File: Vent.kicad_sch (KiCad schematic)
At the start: 11 parts, among them J2 B2B-XH-A_LF__SN_, J3 Conn_01x03_Pin, SW1 SW_Push, U1 ESP32-H2-MINI-1

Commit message: feat: Remove BOOT pin connection
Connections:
- net IO9: no longer names the net of U1.23 (GPIO9)
- no-connect marks 12 -> 13
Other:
- sheet ExternalAutoprogramming (Low-Profile Female) ports: added none; removed BOOT
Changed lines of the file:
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@@
+	)
+	(no_connect
+		(at 181.61 87.63)
 	)
 	(no_connect
@@
 	(label "IO12"
 		(at 181.61 90.17 0)
-		(effects
-			(font
-				(size 1.27 1.27)
-			)
-			(justify left bottom)
-		)
-	)
-	(label "IO9"
-		(at 24.13 22.86 180)
-		(effects
-			(font
-				(size 1.27 1.27)
-			)
-			(justify right bottom)
-		)
-	)
-	(label "IO9"
-		(at 181.61 87.63 0)
 		(effects
 			(font
@@
 			)
 		)
-		(pin "BOOT" bidirectional
-			(at 24.13 22.86 180)
-			(effects
-				(font
-					(size 1.27 1.27)
-				)
-				(justify left)
-			)
-		)

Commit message: feat: Disconnect EN pin from external autoprogramming
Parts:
- added C4: 1uF, Capacitor_SMD:C_1206_3216Metric, symbol Device:C_Small
- added R4: 10k, Resistor_SMD:R_0201_0603Metric, symbol Device:R
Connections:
- net +3.3V: now also R4.2
- net EN: no longer U1.8 (EN)
- net GND: now also C4.1
- new net: C4.2, R4.1, U1.8 (EN)

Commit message: feat: Replace autoprogramming symbol with Conn_02x03
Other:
- sheet ExternalAutoprogramming (Low-Profile Female) ports: added none; removed EN
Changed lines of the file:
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@@
-		)
-	)
-	(label "EN"
-		(at 24.13 25.4 180)
-		(effects
-			(font
-				(size 1.27 1.27)
-			)
-			(justify right bottom)
 		)
 	)
@@
 			)
 		)
-		(pin "EN" input
-			(at 24.13 25.4 180)
-			(effects
-				(font
-					(size 1.27 1.27)
-				)
-				(justify left)
-			)
-		)

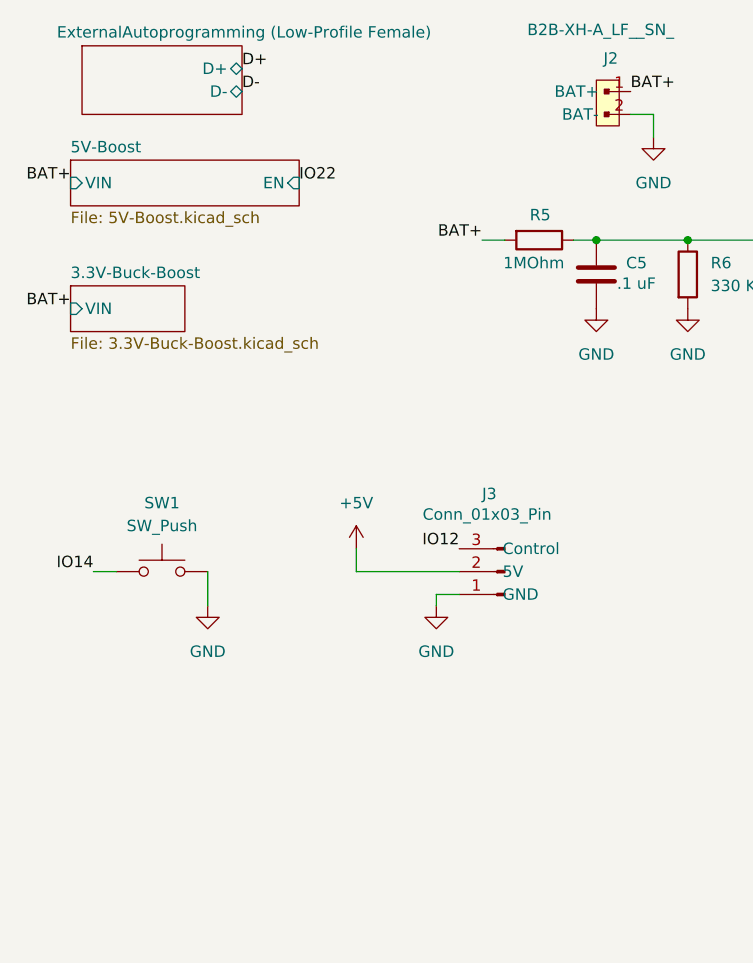
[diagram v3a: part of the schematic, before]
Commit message: feat: Remove autoprogramming schematic
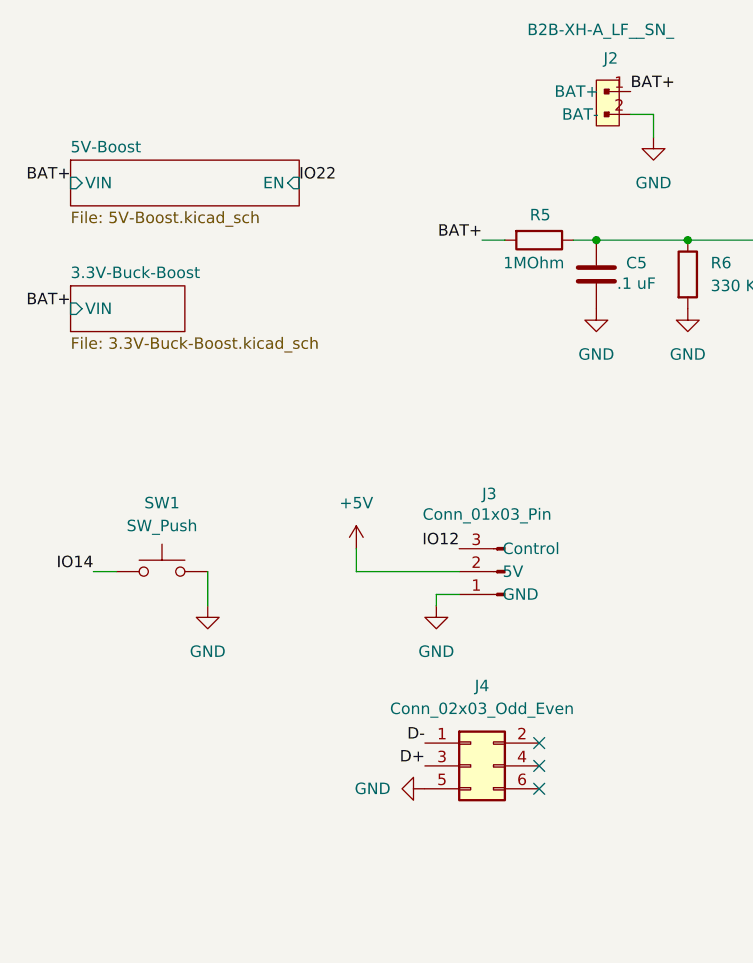
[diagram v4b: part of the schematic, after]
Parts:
- added J4: Conn_02x03_Odd_Even, Connector:Tag-Connect_TC2030-IDC-NL_2x03_P1.27mm_Vertical, symbol Connector_Generic:Conn_02x03_Odd_Even
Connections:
- net D+: now also J4.3 (Pin_3)
- net D-: now also J4.1 (Pin_1)
- net GND: now also J4.5 (Pin_5)
- no-connect marks 13 -> 16
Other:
- removed sheet ExternalAutoprogramming (Low-Profile Female)
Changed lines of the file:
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@@
+	)
+	(no_connect
+		(at 74.93 102.87)
 	)
 	(no_connect
 		(at 181.61 45.72)
+	)
+	(no_connect
+		(at 74.93 97.79)
+	)
+	(no_connect
+		(at 74.93 100.33)
 	)
 	(no_connect
@@
 	)
 	(label "D+"
-		(at 41.91 22.86 0)
+		(at 62.23 100.33 180)
 		(effects
 			(font
 				(size 1.27 1.27)
 			)
-			(justify left bottom)
+			(justify right bottom)
 		)
 	)
@@
 	)
 	(label "D-"
-		(at 41.91 25.4 0)
+		(at 62.23 97.79 180)
 		(effects
 			(font
 				(size 1.27 1.27)
 			)
-			(justify left bottom)
+			(justify right bottom)
 		)
 	)
@@
 	)
 	(symbol
+		(lib_name "Conn_02x03_Odd_Even_1")
+		(lib_id "Connector_Generic:Conn_02x03_Odd_Even")
+		(at 67.31 100.33 0)
+		(unit 1)
+		(body_style 1)
+		(exclude_from_sim no)
+		(in_bom yes)
+		(on_board yes)
+		(in_pos_files yes)
+		(dnp no)
+		(fields_autoplaced yes)
+		(property "Reference" "J4"
+			(at 68.58 91.44 0)
+			(show_name no)
+			(do_not_autoplace no)
+			(effects
+				(font
+					(size 1.27 1.27)
+				)
+			)
+		)
+		(property "Value" "Conn_02x03_Odd_Even"
+			(at 68.58 93.98 0)
+			(show_name no)
+			(do_not_autoplace no)
+			(effects
+				(font
+					(size 1.27 1.27)
+				)
+			)
+		)
+		(property "Footprint" "Connector:Tag-Connect_TC2030-IDC-NL_2x03_P1.27mm_Vertical"
+			(at 67.31 100.33 0)
+			(hide yes)
+			(show_name no)
+			(do_not_autoplace no)
+			(effects
+				(font
+					(size 1.27 1.27)
+				)
+			)
+		)
+		(property "Datasheet" ""
+			(at 67.31 100.33 0)
+			(hide yes)
+			(show_name no)
+			(do_not_autoplace no)
+			(effects
+				(font
+					(size 1.27 1.27)
+				)
+			)
+		)
+		(property "Description" "Generic connector, double row, 02x03, odd/even pin numbering scheme (row 1 odd numbers, row 2 even numbers), script generated (kicad-library-utils/schlib/autogen/connector/)"
+			(at 67.31 100.33 0)
+			(hide yes)
+			(show_name no)
+			(do_not_autoplace no)
+			(effects
+				(font
+					(size 1.27 1.27)
+				)
+			)
+		)
+		(pin "4"
+		)
+		(pin "5"
+		)
+		(pin "2"
+		)
+		(pin "6"
+		)
+		(pin "1"
+		)
+		(pin "3"
+		)
+		(instances
+			(project "Vent"
+				(path "/44080430-3c3a-4a58-87da-65c26034d41d"
+					(reference "J4")
+					(unit 1)
+				)
+			)
+		)
+	)
+	(symbol
 		(lib_id "power:GND")
 		(at 91.44 49.53 0)
@@
 				(path "/44080430-3c3a-4a58-87da-65c26034d41d"
 					(reference "#PWR04")
+					(unit 1)
+				)
+			)
+		)
+	)
+	(symbol
+		(lib_id "power:GND")
+		(at 62.23 102.87 270)
+		(mirror x)
+		(unit 1)
+		(body_style 1)
+		(exclude_from_sim no)
+		(in_bom yes)
+		(on_board yes)
+		(in_pos_files yes)
+		(dnp no)
+		(fields_autoplaced yes)
+		(property "Reference" "#PWR015"
+			(at 55.88 102.87 0)
+			(hide yes)
+			(show_name no)
+			(do_not_autoplace no)
+			(effects
+				(font
+					(size 1.27 1.27)
+				)
+			)
+		)
+		(property "Value" "GND"
+			(at 58.42 102.8699 90)
+			(show_name no)
+			(do_not_autoplace no)
+			(effects
+				(font
+					(size 1.27 1.27)
+				)
+				(justify right)
+			)
+		)
+		(property "Footprint" ""
+			(at 62.23 102.87 0)
+			(hide yes)
+			(show_name no)
+			(do_not_autoplace no)
+			(effects
+				(font
+					(size 1.27 1.27)
+				)
+			)
+		)
+		(property "Datasheet" ""
+			(at 62.23 102.87 0)
+			(hide yes)
+			(show_name no)
+			(do_not_autoplace no)
+			(effects
+				(font
+					(size 1.27 1.27)
+				)
+			)
+		)
+		(property "Description" "Power symbol creates a global label with name \"GND\" , ground"
+			(at 62.23 102.87 0)
+			(hide yes)
+			(show_name no)
+			(do_not_autoplace no)
+			(effects
+				(font
+					(size 1.27 1.27)
+				)
+			)
+		)
+		(pin "1"
+		)
+		(instances
+			(project "Vent"
+				(path "/44080430-3c3a-4a58-87da-65c26034d41d"
+					(reference "#PWR015")
 					(unit 1)
 				)
@@
 				)
 			)
-		)
-	)
-	(sheet
-		(at 24.13 20.32)
-		(size 17.78 7.62)
-		(exclude_from_sim no)
-		(in_bom yes)
-		(on_board yes)
-		(dnp no)
-		(stroke
-			(width 0.1524)
-			(type solid)
-		)
-		(fill
-			(color 255 255 194 1)
-		)
-		(property "Sheetname" "ExternalAutoprogramming (Low-Profile Female)"
-			(at 21.336 19.558 0)
-			(show_name no)
-			(do_not_autoplace no)
-			(effects
-				(font
-					(size 1.27 1.27)
-				)
-				(justify left bottom)
-			)
-		)
-		(property "Sheetfile" "ExternalAutoprogramming.kicad_sch"
-			(at 12.446 28.448 0)
-			(hide yes)
-			(show_name no)
-			(do_not_autoplace no)
-			(effects
-				(font
-					(size 1.27 1.27)
-				)
-				(justify left top)
-			)
-		)
-		(pin "D+" bidirectional
-			(at 41.91 22.86 0)
-			(effects
-				(font
-					(size 1.27 1.27)
-				)
-				(justify right)
-			)
-		)
-		(pin "D-" bidirectional
-			(at 41.91 25.4 0)
-			(effects
-				(font
-					(size 1.27 1.27)
-				)
-				(justify right)
-			)
-		)
-		(instances
-			(project "Vent"
-				(path "/44080430-3c3a-4a58-87da-65c26034d41d"
-					(page "2")
-				)
-			)

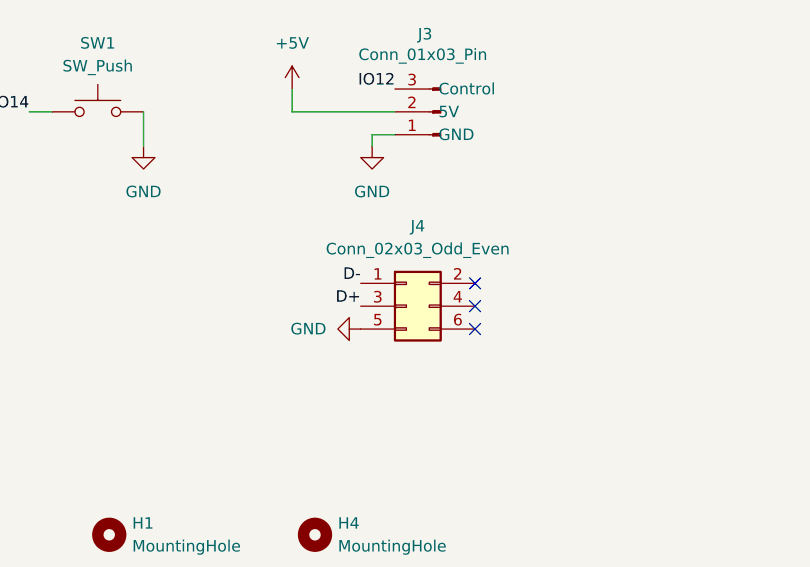
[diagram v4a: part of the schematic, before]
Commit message: feat: Use 1x3 male pin header rather than Tag-Connect
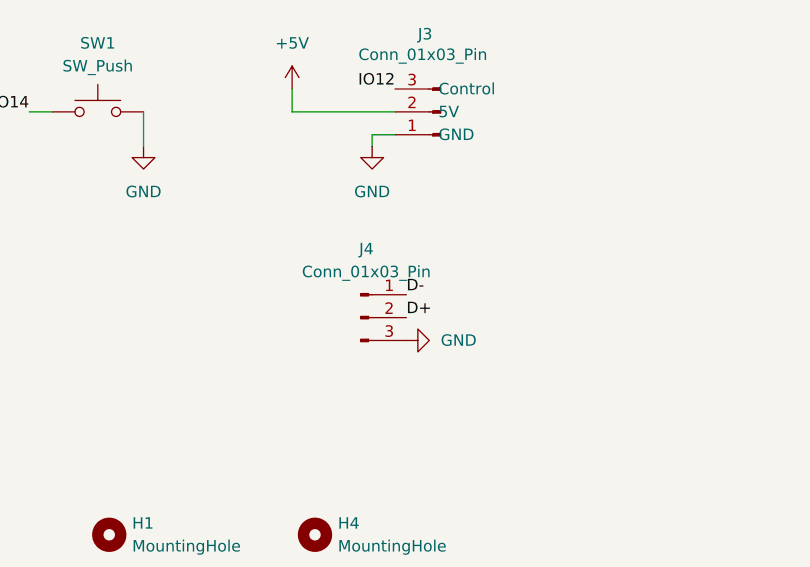
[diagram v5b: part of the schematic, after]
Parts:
- removed J4: Conn_02x03_Odd_Even, Connector:Tag-Connect_TC2030-IDC-NL_2x03_P1.27mm_Vertical, symbol Connector_Generic:Conn_02x03_Odd_Even
- added J4: Conn_01x03_Pin, Connector_PinHeader_2.54mm:PinHeader_1x03_P2.54mm_Vertical, symbol Connector:Conn_01x03_Pin
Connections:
- net D+: now also J4.2 (Pin_2)
- net D-: now also J4.1 (Pin_1)
- net GND: now also J4.3 (Pin_3)
- no-connect marks 16 -> 13
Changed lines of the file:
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@@
-	)
-	(no_connect
-		(at 74.93 102.87)
 	)
 	(no_connect
 		(at 181.61 45.72)
-	)
-	(no_connect
-		(at 74.93 97.79)
-	)
-	(no_connect
-		(at 74.93 100.33)
 	)
 	(no_connect
@@
 		)
 	)
-	(label "D+"
-		(at 62.23 100.33 180)
-		(effects
-			(font
-				(size 1.27 1.27)
-			)
-			(justify right bottom)
-		)
-	)
 	(label "IO14"
 		(at 111.76 55.88 180)
@@
 		)
 	)
+	(label "D-"
+		(at 67.31 99.06 0)
+		(effects
+			(font
+				(size 1.27 1.27)
+			)
+			(justify left bottom)
+		)
+	)
 	(label "IO12"
 		(at 181.61 90.17 0)
@@
 	)
 	(label "D-"
-		(at 62.23 97.79 180)
-		(effects
-			(font
-				(size 1.27 1.27)
-			)
-			(justify right bottom)
-		)
-	)
-	(label "D-"
 		(at 181.61 59.69 0)
 		(effects
@@
 			)
 			(justify right bottom)
+		)
+	)
+	(label "D+"
+		(at 67.31 101.6 0)
+		(effects
+			(font
+				(size 1.27 1.27)
+			)
+			(justify left bottom)
 		)
 	)
@@
 	(symbol
 		(lib_id "power:GND")
+		(at 67.31 104.14 90)
+		(mirror x)
+		(unit 1)
+		(body_style 1)
+		(exclude_from_sim no)
+		(in_bom yes)
+		(on_board yes)
+		(in_pos_files yes)
+		(dnp no)
+		(fields_autoplaced yes)
+		(property "Reference" "#PWR020"
+			(at 73.66 104.14 0)
+			(hide yes)
+			(show_name no)
+			(do_not_autoplace no)
+			(effects
+				(font
+					(size 1.27 1.27)
+				)
+			)
+		)
+		(property "Value" "GND"
+			(at 71.12 104.1399 90)
+			(show_name no)
+			(do_not_autoplace no)
+			(effects
+				(font
+					(size 1.27 1.27)
+				)
+				(justify right)
+			)
+		)
+		(property "Footprint" ""
+			(at 67.31 104.14 0)
+			(hide yes)
+			(show_name no)
+			(do_not_autoplace no)
+			(effects
+				(font
+					(size 1.27 1.27)
+				)
+			)
+		)
+		(property "Datasheet" ""
+			(at 67.31 104.14 0)
+			(hide yes)
+			(show_name no)
+			(do_not_autoplace no)
+			(effects
+				(font
+					(size 1.27 1.27)
+				)
+			)
+		)
+		(property "Description" "Power symbol creates a global label with name \"GND\" , ground"
+			(at 67.31 104.14 0)
+			(hide yes)
+			(show_name no)
+			(do_not_autoplace no)
+			(effects
+				(font
+					(size 1.27 1.27)
+				)
+			)
+		)
+		(pin "1"
+		)
+		(instances
+			(project "Vent"
+				(path "/44080430-3c3a-4a58-87da-65c26034d41d"
+					(reference "#PWR020")
+					(unit 1)
+				)
+			)
+		)
+	)
+	(symbol
+		(lib_id "power:GND")
 		(at 147.32 95.25 0)
 		(unit 1)
@@
 	)
 	(symbol
-		(lib_name "Conn_02x03_Odd_Even_1")
-		(lib_id "Connector_Generic:Conn_02x03_Odd_Even")
-		(at 67.31 100.33 0)
-		(unit 1)
-		(body_style 1)
-		(exclude_from_sim no)
-		(in_bom yes)
-		(on_board yes)
-		(in_pos_files yes)
-		(dnp no)
-		(fields_autoplaced yes)
-		(property "Reference" "J4"
-			(at 68.58 91.44 0)
-			(show_name no)
-			(do_not_autoplace no)
-			(effects
-				(font
-					(size 1.27 1.27)
-				)
-			)
-		)
-		(property "Value" "Conn_02x03_Odd_Even"
-			(at 68.58 93.98 0)
-			(show_name no)
-			(do_not_autoplace no)
-			(effects
-				(font
-					(size 1.27 1.27)
-				)
-			)
-		)
-		(property "Footprint" "Connector:Tag-Connect_TC2030-IDC-NL_2x03_P1.27mm_Vertical"
-			(at 67.31 100.33 0)
-			(hide yes)
-			(show_name no)
-			(do_not_autoplace no)
-			(effects
-				(font
-					(size 1.27 1.27)
-				)
-			)
-		)
-		(property "Datasheet" ""
-			(at 67.31 100.33 0)
-			(hide yes)
-			(show_name no)
-			(do_not_autoplace no)
-			(effects
-				(font
-					(size 1.27 1.27)
-				)
-			)
-		)
-		(property "Description" "Generic connector, double row, 02x03, odd/even pin numbering scheme (row 1 odd numbers, row 2 even numbers), script generated (kicad-library-utils/schlib/autogen/connector/)"
-			(at 67.31 100.33 0)
-			(hide yes)
-			(show_name no)
-			(do_not_autoplace no)
-			(effects
-				(font
-					(size 1.27 1.27)
-				)
-			)
-		)
-		(pin "4"
-		)
-		(pin "5"
-		)
-		(pin "2"
-		)
-		(pin "6"
-		)
-		(pin "1"
-		)
-		(pin "3"
-		)
-		(instances
-			(project "Vent"
-				(path "/44080430-3c3a-4a58-87da-65c26034d41d"
-					(reference "J4")
-					(unit 1)
-				)
-			)
-		)
-	)
-	(symbol
 		(lib_id "power:GND")
 		(at 91.44 49.53 0)
@@
 	)
 	(symbol
-		(lib_id "power:GND")
-		(at 62.23 102.87 270)
-		(mirror x)
+		(lib_name "Conn_01x03_Pin_1")
+		(lib_id "Connector:Conn_01x03_Pin")
+		(at 62.23 101.6 0)
 		(unit 1)
 		(body_style 1)
@@
 		(dnp no)
 		(fields_autoplaced yes)
-		(property "Reference" "#PWR015"
-			(at 55.88 102.87 0)
-			(hide yes)
-			(show_name no)
-			(do_not_autoplace no)
-			(effects
-				(font
-					(size 1.27 1.27)
-				)
-			)
-		)
-		(property "Value" "GND"
-			(at 58.42 102.8699 90)
-			(show_name no)
-			(do_not_autoplace no)
-			(effects
-				(font
-					(size 1.27 1.27)
-				)
-				(justify right)
-			)
-		)
-		(property "Footprint" ""
-			(at 62.23 102.87 0)
+		(property "Reference" "J4"
+			(at 62.865 93.98 0)
+			(show_name no)
+			(do_not_autoplace no)
+			(effects
+				(font
+					(size 1.27 1.27)
+				)
+			)
+		)
+		(property "Value" "Conn_01x03_Pin"
+			(at 62.865 96.52 0)
+			(show_name no)
+			(do_not_autoplace no)
+			(effects
+				(font
+					(size 1.27 1.27)
+				)
+			)
+		)
+		(property "Footprint" "Connector_PinHeader_2.54mm:PinHeader_1x03_P2.54mm_Vertical"
+			(at 62.23 101.6 0)
 			(hide yes)
 			(show_name no)
@@
 		)
 		(property "Datasheet" ""
-			(at 62.23 102.87 0)
-			(hide yes)
-			(show_name no)
-			(do_not_autoplace no)
-			(effects
-				(font
-					(size 1.27 1.27)
-				)
-			)
-		)
-		(property "Description" "Power symbol creates a global label with name \"GND\" , ground"
-			(at 62.23 102.87 0)
-			(hide yes)
-			(show_name no)
-			(do_not_autoplace no)
-			(effects
-				(font
-					(size 1.27 1.27)
-				)
-			)
+			(at 62.23 101.6 0)
+			(hide yes)
+			(show_name no)
+			(do_not_autoplace no)
+			(effects
+				(font
+					(size 1.27 1.27)
+				)
+			)
+		)
+		(property "Description" "Generic connector, single row, 01x03, script generated"
+			(at 62.23 101.6 0)
+			(hide yes)
+			(show_name no)
+			(do_not_autoplace no)
+			(effects
+				(font
+					(size 1.27 1.27)
+				)
+			)
+		)
+		(pin "2"
+		)
+		(pin "3"
 		)
 		(pin "1"
@@
 			(project "Vent"
 				(path "/44080430-3c3a-4a58-87da-65c26034d41d"
-					(reference "#PWR015")
+					(reference "J4")
 					(unit 1)
 				)
